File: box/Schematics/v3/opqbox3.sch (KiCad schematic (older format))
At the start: 2 parts, among them J1 Conn_01x02_Male, J2 Conn_01x02_Male

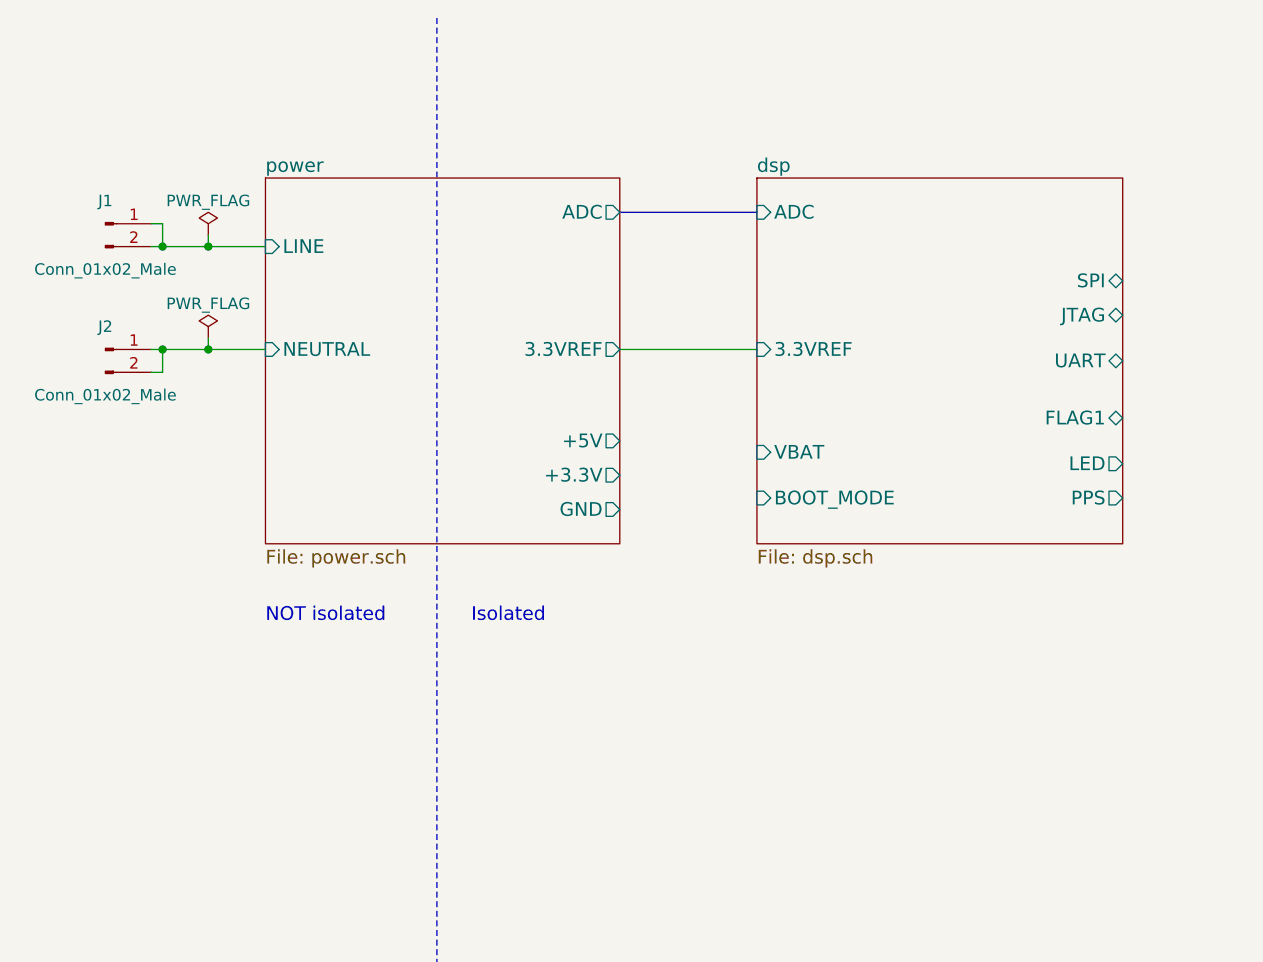
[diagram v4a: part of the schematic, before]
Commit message: create connectors sheet
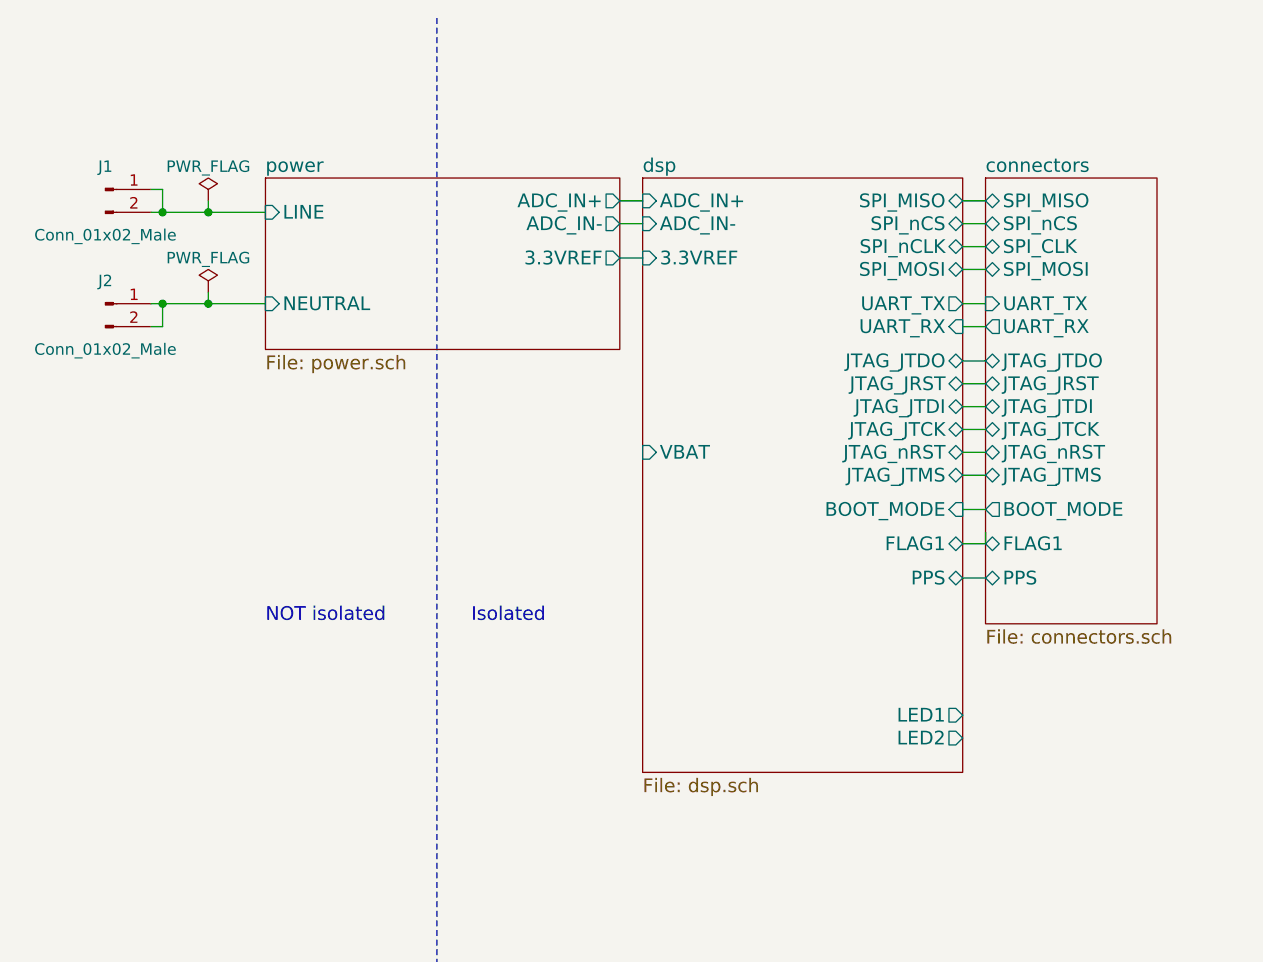
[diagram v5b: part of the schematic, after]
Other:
- moved on the sheet: J1, J2
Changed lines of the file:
@@
 LIBS:power
 LIBS:conn
-LIBS:contrib
-LIBS:stm32
 LIBS:opqbox3-cache
 EELAYER 25 0
@@
 $Descr A4 11693 8268
 encoding utf-8
-Sheet 1 3
+Sheet 1 4
 Title ""
 Date ""
@@
 $EndDescr
 $Sheet
-S 2150 1200 1550 1600
+S 2150 1200 1550 750
 U 5A829EE9
 F0 "power" 60
 F1 "power.sch" 60
-F2 "LINE" I L 2150 1500 60
-F3 "NEUTRAL" I L 2150 1950 60
-F4 "+3.3V" O R 3700 2500 60
-F5 "+5V" O R 3700 2350 60
-F6 "GND" O R 3700 2650 60
-F7 "3.3VREF" O R 3700 1950 60
-F8 "ADC" O R 3700 1350 60
+F2 "LINE" I L 2150 1350 60
+F3 "NEUTRAL" I L 2150 1750 60
+F4 "3.3VREF" O R 3700 1550 60
+F5 "ADC_IN-" O R 3700 1400 60
+F6 "ADC_IN+" O R 3700 1300 60
 $EndSheet
-Wire Notes Line
-	2900 500  2900 7750
 $Comp
 L Conn_01x02_Male J1
 U 1 1 5A82EE79
-P 1450 1400
-F 0 "J1" H 1450 1500 50  0000 C CNN
-F 1 "Conn_01x02_Male" H 1450 1200 50  0000 C CNN
-F 2 "" H 1450 1400 50  0001 C CNN
-F 3 "" H 1450 1400 50  0001 C CNN
-	1    1450 1400
+P 1450 1250
+F 0 "J1" H 1450 1350 50  0000 C CNN
+F 1 "Conn_01x02_Male" H 1450 1050 50  0000 C CNN
+F 2 "" H 1450 1250 50  0001 C CNN
+F 3 "" H 1450 1250 50  0001 C CNN
+	1    1450 1250
 	1    0    0    -1
 $EndComp
@@
 L Conn_01x02_Male J2
 U 1 1 5A82EEC2
-P 1450 1950
-F 0 "J2" H 1450 2050 50  0000 C CNN
-F 1 "Conn_01x02_Male" H 1450 1750 50  0000 C CNN
-F 2 "" H 1450 1950 50  0001 C CNN
-F 3 "" H 1450 1950 50  0001 C CNN
-	1    1450 1950
+P 1450 1750
+F 0 "J2" H 1450 1850 50  0000 C CNN
+F 1 "Conn_01x02_Male" H 1450 1550 50  0000 C CNN
+F 2 "" H 1450 1750 50  0001 C CNN
+F 3 "" H 1450 1750 50  0001 C CNN
+	1    1450 1750
 	1    0    0    -1
 $EndComp
-Wire Wire Line
-	1650 1400 1700 1400
-Wire Wire Line
-	1700 1400 1700 1500
-Wire Wire Line
-	1650 1500 2150 1500
-Connection ~ 1700 1500
-Wire Wire Line
-	1650 2050 1700 2050
-Wire Wire Line
-	1700 2050 1700 1950
-Wire Wire Line
-	1650 1950 2150 1950
-Connection ~ 1700 1950
 $Comp
 L PWR_FLAG #FLG01
 U 1 1 5A82F319
-P 1900 1450
-F 0 "#FLG01" H 1900 1525 50  0001 C CNN
-F 1 "PWR_FLAG" H 1900 1600 50  0000 C CNN
-F 2 "" H 1900 1450 50  0001 C CNN
-F 3 "" H 1900 1450 50  0001 C CNN
-	1    1900 1450
+P 1900 1300
+F 0 "#FLG01" H 1900 1375 50  0001 C CNN
+F 1 "PWR_FLAG" H 1900 1450 50  0000 C CNN
+F 2 "" H 1900 1300 50  0001 C CNN
+F 3 "" H 1900 1300 50  0001 C CNN
+	1    1900 1300
 	1    0    0    -1
 $EndComp
@@
 L PWR_FLAG #FLG02
 U 1 1 5A82F35B
-P 1900 1900
-F 0 "#FLG02" H 1900 1975 50  0001 C CNN
-F 1 "PWR_FLAG" H 1900 2050 50  0000 C CNN
-F 2 "" H 1900 1900 50  0001 C CNN
-F 3 "" H 1900 1900 50  0001 C CNN
-	1    1900 1900
+P 1900 1700
+F 0 "#FLG02" H 1900 1775 50  0001 C CNN
+F 1 "PWR_FLAG" H 1900 1850 50  0000 C CNN
+F 2 "" H 1900 1700 50  0001 C CNN
+F 3 "" H 1900 1700 50  0001 C CNN
+	1    1900 1700
 	1    0    0    -1
 $EndComp
-Wire Wire Line
-	1900 1900 1900 1950
-Connection ~ 1900 1950
-Wire Wire Line
-	1900 1450 1900 1500
-Connection ~ 1900 1500
 Text Notes 3050 3150 0    60   ~ 0
 Isolated
 Text Notes 2150 3150 0    60   ~ 0
 NOT isolated
+Wire Notes Line
+	2900 500  2900 7750
+Wire Wire Line
+	1650 1250 1700 1250
+Wire Wire Line
+	1700 1250 1700 1350
+Wire Wire Line
+	1650 1350 2150 1350
+Connection ~ 1700 1350
+Wire Wire Line
+	1650 1850 1700 1850
+Wire Wire Line
+	1700 1850 1700 1750
+Wire Wire Line
+	1650 1750 2150 1750
+Connection ~ 1700 1750
+Wire Wire Line
+	1900 1700 1900 1750
+Connection ~ 1900 1750
+Wire Wire Line
+	1900 1300 1900 1350
+Connection ~ 1900 1350
 $Sheet
-S 4300 1200 1600 1600
+S 5300 1200 750  1950
+U 5A8506F3
+F0 "connectors" 60
+F1 "connectors.sch" 60
+F2 "SPI_MISO" B L 5300 1300 60
+F3 "SPI_MOSI" B L 5300 1600 60
+F4 "SPI_nCS" B L 5300 1400 60
+F5 "SPI_CLK" B L 5300 1500 60
+F6 "JTAG_nRST" B L 5300 2400 60
+F7 "BOOT_MODE" O L 5300 2650 60
+F8 "UART_RX" O L 5300 1850 60
+F9 "UART_TX" I L 5300 1750 60
+F10 "FLAG1" B L 5300 2800 60
+F11 "JTAG_JRST" B L 5300 2100 60
+F12 "JTAG_JTCK" B L 5300 2300 60
+F13 "JTAG_JTDI" B L 5300 2200 60
+F14 "JTAG_JTDO" B L 5300 2000 60
+F15 "JTAG_JTMS" B L 5300 2500 60
+F16 "PPS" B L 5300 2950 60
+$EndSheet
+Wire Wire Line
+	5300 2750 5300 2800
+Wire Wire Line
+	5300 2800 5200 2800
+Wire Wire Line
+	5200 2650 5300 2650
+Wire Wire Line
+	5200 2500 5300 2500
+Wire Wire Line
+	5200 2400 5300 2400
+Wire Wire Line
+	5200 2300 5300 2300
+Wire Wire Line
+	5200 2200 5300 2200
+Wire Wire Line
+	5200 2100 5300 2100
+Wire Wire Line
+	5200 2000 5300 2000
+Wire Wire Line
+	5200 1850 5300 1850
+Wire Wire Line
+	5300 1750 5200 1750
+Wire Wire Line
+	5200 1600 5300 1600
+Wire Wire Line
+	5200 1500 5300 1500
+Wire Wire Line
+	5200 1400 5300 1400
+Wire Wire Line
+	5200 1300 5300 1300
+$Sheet
+S 3800 1200 1400 2600
 U 5A835DDE
 F0 "dsp" 60
 F1 "dsp.sch" 60
-F2 "3.3VREF" I L 4300 1950 60
-F3 "SPI" B R 5900 1650 60
-F4 "JTAG" B R 5900 1800 60
-F5 "UART" B R 5900 2000 60
-F6 "PPS" O R 5900 2600 60
-F7 "LED" O R 5900 2450 60
-F8 "BOOT_MODE" I L 4300 2600 60
-F9 "VBAT" I L 4300 2400 60
-F10 "FLAG1" B R 5900 2250 60
-F11 "ADC" I L 4300 1350 60
+F2 "BOOT_MODE" I R 5200 2650 60
+F3 "VBAT" I L 3800 2400 60
+F4 "SPI_MISO" B R 5200 1300 60
+F5 "LED1" O R 5200 3550 60
+F6 "FLAG1" B R 5200 2800 60
+F7 "ADC_IN+" I L 3800 1300 60
+F8 "SPI_nCS" B R 5200 1400 60
+F9 "SPI_nCLK" B R 5200 1500 60
+F10 "SPI_MOSI" B R 5200 1600 60
+F11 "ADC_IN-" I L 3800 1400 60
+F12 "LED2" O R 5200 3650 60
+F13 "JTAG_JTDO" B R 5200 2000 60
+F14 "JTAG_JRST" B R 5200 2100 60
+F15 "JTAG_JTDI" B R 5200 2200 60
+F16 "JTAG_JTCK" B R 5200 2300 60
+F17 "JTAG_nRST" B R 5200 2400 60
+F18 "JTAG_JTMS" B R 5200 2500 60
+F19 "3.3VREF" I L 3800 1550 60
+F20 "UART_RX" I R 5200 1850 60
+F21 "UART_TX" O R 5200 1750 60
+F22 "PPS" B R 5200 2950 60
 $EndSheet
 Wire Wire Line
-	3700 1950 4300 1950
-Wire Bus Line
-	3700 1350 4300 1350
+	5200 2950 5300 2950
+Wire Wire Line
+	3700 1300 3800 1300
+Wire Wire Line
+	3700 1400 3800 1400
+Wire Wire Line
+	3700 1550 3800 1550
 $EndSCHEMATC

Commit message: create io schematics
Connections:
- no-connect marks 0 -> 1
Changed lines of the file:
@@
 $EndDescr
 $Sheet
-S 2150 1200 1550 750
+S 2150 1200 1050 750
 U 5A829EE9
 F0 "power" 60
@@
 F2 "LINE" I L 2150 1350 60
 F3 "NEUTRAL" I L 2150 1750 60
-F4 "3.3VREF" O R 3700 1550 60
-F5 "ADC_IN-" O R 3700 1400 60
-F6 "ADC_IN+" O R 3700 1300 60
+F4 "3.3VREF" O R 3200 1550 60
+F5 "ADC_IN-" O R 3200 1400 60
+F6 "ADC_IN+" O R 3200 1300 60
 $EndSheet
 $Comp
@@
 	1    0    0    -1
 $EndComp
-Text Notes 3050 3150 0    60   ~ 0
+Text Notes 2800 800  0    60   ~ 0
 Isolated
-Text Notes 2150 3150 0    60   ~ 0
+Text Notes 2050 800  0    60   ~ 0
 NOT isolated
+$Sheet
+S 4800 1200 750  2300
+U 5A8506F3
+F0 "io" 60
+F1 "io.sch" 60
+F2 "SPI_MISO" B L 4800 1300 60
+F3 "SPI_MOSI" B L 4800 1600 60
+F4 "SPI_nCS" B L 4800 1400 60
+F5 "SPI_CLK" B L 4800 1500 60
+F6 "JTAG_nRST" B L 4800 2400 60
+F7 "BOOT_MODE" O L 4800 2650 60
+F8 "UART_RX" O L 4800 1850 60
+F9 "UART_TX" I L 4800 1750 60
+F10 "FLAG1" B L 4800 2800 60
+F11 "JTAG_JRST" B L 4800 2100 60
+F12 "JTAG_JTCK" B L 4800 2300 60
+F13 "JTAG_JTDI" B L 4800 2200 60
+F14 "JTAG_JTDO" B L 4800 2000 60
+F15 "JTAG_JTMS" B L 4800 2500 60
+F16 "PPS" B L 4800 2950 60
+F17 "LED1" I L 4800 3300 60
+F18 "LED2" I L 4800 3400 60
+$EndSheet
+$Sheet
+S 3300 1200 1400 2600
+U 5A835DDE
+F0 "dsp" 60
+F1 "dsp.sch" 60
+F2 "BOOT_MODE" I R 4700 2650 60
+F3 "VBAT" I L 3300 1850 60
+F4 "SPI_MISO" B R 4700 1300 60
+F5 "LED1" O R 4700 3300 60
+F6 "FLAG1" B R 4700 2800 60
+F7 "ADC_IN+" I L 3300 1300 60
+F8 "SPI_nCS" B R 4700 1400 60
+F9 "SPI_nCLK" B R 4700 1500 60
+F10 "SPI_MOSI" B R 4700 1600 60
+F11 "ADC_IN-" I L 3300 1400 60
+F12 "LED2" O R 4700 3400 60
+F13 "JTAG_JTDO" B R 4700 2000 60
+F14 "JTAG_JRST" B R 4700 2100 60
+F15 "JTAG_JTDI" B R 4700 2200 60
+F16 "JTAG_JTCK" B R 4700 2300 60
+F17 "JTAG_nRST" B R 4700 2400 60
+F18 "JTAG_JTMS" B R 4700 2500 60
+F19 "3.3VREF" I L 3300 1550 60
+F20 "UART_RX" I R 4700 1850 60
+F21 "UART_TX" O R 4700 1750 60
+F22 "PPS" B R 4700 2950 60
+$EndSheet
 Wire Notes Line
-	2900 500  2900 7750
+	2700 500  2700 7750
 Wire Wire Line
 	1650 1250 1700 1250
@@
 	1900 1300 1900 1350
 Connection ~ 1900 1350
-$Sheet
-S 5300 1200 750  1950
-U 5A8506F3
-F0 "connectors" 60
-F1 "connectors.sch" 60
-F2 "SPI_MISO" B L 5300 1300 60
-F3 "SPI_MOSI" B L 5300 1600 60
-F4 "SPI_nCS" B L 5300 1400 60
-F5 "SPI_CLK" B L 5300 1500 60
-F6 "JTAG_nRST" B L 5300 2400 60
-F7 "BOOT_MODE" O L 5300 2650 60
-F8 "UART_RX" O L 5300 1850 60
-F9 "UART_TX" I L 5300 1750 60
-F10 "FLAG1" B L 5300 2800 60
-F11 "JTAG_JRST" B L 5300 2100 60
-F12 "JTAG_JTCK" B L 5300 2300 60
-F13 "JTAG_JTDI" B L 5300 2200 60
-F14 "JTAG_JTDO" B L 5300 2000 60
-F15 "JTAG_JTMS" B L 5300 2500 60
-F16 "PPS" B L 5300 2950 60
-$EndSheet
 Wire Wire Line
-	5300 2750 5300 2800
+	4800 2750 4800 2800
 Wire Wire Line
-	5300 2800 5200 2800
+	4800 2800 4700 2800
 Wire Wire Line
-	5200 2650 5300 2650
+	4700 2650 4800 2650
 Wire Wire Line
-	5200 2500 5300 2500
+	4700 2500 4800 2500
 Wire Wire Line
-	5200 2400 5300 2400
+	4700 2400 4800 2400
 Wire Wire Line
-	5200 2300 5300 2300
+	4700 2300 4800 2300
 Wire Wire Line
-	5200 2200 5300 2200
+	4700 2200 4800 2200
 Wire Wire Line
-	5200 2100 5300 2100
+	4700 2100 4800 2100
 Wire Wire Line
-	5200 2000 5300 2000
+	4700 2000 4800 2000
 Wire Wire Line
-	5200 1850 5300 1850
+	4700 1850 4800 1850
 Wire Wire Line
-	5300 1750 5200 1750
+	4800 1750 4700 1750
 Wire Wire Line
-	5200 1600 5300 1600
+	4700 1600 4800 1600
 Wire Wire Line
-	5200 1500 5300 1500
+	4700 1500 4800 1500
 Wire Wire Line
-	5200 1400 5300 1400
+	4700 1400 4800 1400
 Wire Wire Line
-	5200 1300 5300 1300
-$Sheet
-S 3800 1200 1400 2600
-U 5A835DDE
-F0 "dsp" 60
-F1 "dsp.sch" 60
-F2 "BOOT_MODE" I R 5200 2650 60
-F3 "VBAT" I L 3800 2400 60
-F4 "SPI_MISO" B R 5200 1300 60
-F5 "LED1" O R 5200 3550 60
-F6 "FLAG1" B R 5200 2800 60
-F7 "ADC_IN+" I L 3800 1300 60
-F8 "SPI_nCS" B R 5200 1400 60
-F9 "SPI_nCLK" B R 5200 1500 60
-F10 "SPI_MOSI" B R 5200 1600 60
-F11 "ADC_IN-" I L 3800 1400 60
-F12 "LED2" O R 5200 3650 60
-F13 "JTAG_JTDO" B R 5200 2000 60
-F14 "JTAG_JRST" B R 5200 2100 60
-F15 "JTAG_JTDI" B R 5200 2200 60
-F16 "JTAG_JTCK" B R 5200 2300 60
-F17 "JTAG_nRST" B R 5200 2400 60
-F18 "JTAG_JTMS" B R 5200 2500 60
-F19 "3.3VREF" I L 3800 1550 60
-F20 "UART_RX" I R 5200 1850 60
-F21 "UART_TX" O R 5200 1750 60
-F22 "PPS" B R 5200 2950 60
-$EndSheet
+	4700 1300 4800 1300
 Wire Wire Line
-	5200 2950 5300 2950
+	4700 2950 4800 2950
 Wire Wire Line
-	3700 1300 3800 1300
+	3200 1300 3300 1300
 Wire Wire Line
-	3700 1400 3800 1400
+	3200 1400 3300 1400
 Wire Wire Line
-	3700 1550 3800 1550
+	3200 1550 3300 1550
+Wire Wire Line
+	4700 3300 4800 3300
+Wire Wire Line
+	4700 3400 4800 3400
+NoConn ~ 3300 1850
 $EndSCHEMATC

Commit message: start layout
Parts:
- J1, J2: footprint (none) -> opqbox3:FastonTab
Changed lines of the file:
@@
 EESchema Schematic File Version 2
+LIBS:opqbox3-rescue
 LIBS:opqbox3
 LIBS:device
@@
 $EndDescr
 $Sheet
-S 2150 1200 1050 750
+S 2150 1200 1100 750
 U 5A829EE9
 F0 "power" 60
@@
 F2 "LINE" I L 2150 1350 60
 F3 "NEUTRAL" I L 2150 1750 60
-F4 "3.3VREF" O R 3200 1550 60
-F5 "ADC_IN-" O R 3200 1400 60
-F6 "ADC_IN+" O R 3200 1300 60
+F4 "3.3VREF" O R 3250 1550 60
+F5 "ADC_IN-" O R 3250 1400 60
+F6 "ADC_IN+" O R 3250 1300 60
 $EndSheet
-$Comp
-L Conn_01x02_Male J1
-U 1 1 5A82EE79
-P 1450 1250
-F 0 "J1" H 1450 1350 50  0000 C CNN
-F 1 "Conn_01x02_Male" H 1450 1050 50  0000 C CNN
-F 2 "" H 1450 1250 50  0001 C CNN
-F 3 "" H 1450 1250 50  0001 C CNN
-	1    1450 1250
-	1    0    0    -1
-$EndComp
-$Comp
-L Conn_01x02_Male J2
-U 1 1 5A82EEC2
-P 1450 1750
-F 0 "J2" H 1450 1850 50  0000 C CNN
-F 1 "Conn_01x02_Male" H 1450 1550 50  0000 C CNN
-F 2 "" H 1450 1750 50  0001 C CNN
-F 3 "" H 1450 1750 50  0001 C CNN
-	1    1450 1750
-	1    0    0    -1
-$EndComp
 $Comp
 L PWR_FLAG #FLG01
@@
 NOT isolated
 $Sheet
-S 4800 1200 750  2300
+S 4850 1200 750  2300
 U 5A8506F3
 F0 "io" 60
 F1 "io.sch" 60
-F2 "SPI_MISO" B L 4800 1300 60
-F3 "SPI_MOSI" B L 4800 1600 60
-F4 "SPI_nCS" B L 4800 1400 60
-F5 "SPI_CLK" B L 4800 1500 60
-F6 "JTAG_nRST" B L 4800 2400 60
-F7 "BOOT_MODE" O L 4800 2650 60
-F8 "UART_RX" O L 4800 1850 60
-F9 "UART_TX" I L 4800 1750 60
-F10 "FLAG1" B L 4800 2800 60
-F11 "JTAG_JRST" B L 4800 2100 60
-F12 "JTAG_JTCK" B L 4800 2300 60
-F13 "JTAG_JTDI" B L 4800 2200 60
-F14 "JTAG_JTDO" B L 4800 2000 60
-F15 "JTAG_JTMS" B L 4800 2500 60
-F16 "PPS" B L 4800 2950 60
-F17 "LED1" I L 4800 3300 60
-F18 "LED2" I L 4800 3400 60
+F2 "SPI_MISO" B L 4850 1300 60
+F3 "SPI_MOSI" B L 4850 1600 60
+F4 "SPI_nCS" B L 4850 1400 60
+F5 "SPI_CLK" B L 4850 1500 60
+F6 "JTAG_nRST" B L 4850 2400 60
+F7 "BOOT_MODE" O L 4850 2650 60
+F8 "UART_RX" O L 4850 1850 60
+F9 "UART_TX" I L 4850 1750 60
+F10 "FLAG1" B L 4850 2800 60
+F11 "JTAG_JRST" B L 4850 2100 60
+F12 "JTAG_JTCK" B L 4850 2300 60
+F13 "JTAG_JTDI" B L 4850 2200 60
+F14 "JTAG_JTDO" B L 4850 2000 60
+F15 "JTAG_JTMS" B L 4850 2500 60
+F16 "PPS" B L 4850 2950 60
+F17 "LED1" I L 4850 3300 60
+F18 "LED2" I L 4850 3400 60
 $EndSheet
 $Sheet
-S 3300 1200 1400 2600
+S 3350 1200 1400 2600
 U 5A835DDE
 F0 "dsp" 60
 F1 "dsp.sch" 60
-F2 "BOOT_MODE" I R 4700 2650 60
-F3 "VBAT" I L 3300 1850 60
-F4 "SPI_MISO" B R 4700 1300 60
-F5 "LED1" O R 4700 3300 60
-F6 "FLAG1" B R 4700 2800 60
-F7 "ADC_IN+" I L 3300 1300 60
-F8 "SPI_nCS" B R 4700 1400 60
-F9 "SPI_nCLK" B R 4700 1500 60
-F10 "SPI_MOSI" B R 4700 1600 60
-F11 "ADC_IN-" I L 3300 1400 60
-F12 "LED2" O R 4700 3400 60
-F13 "JTAG_JTDO" B R 4700 2000 60
-F14 "JTAG_JRST" B R 4700 2100 60
-F15 "JTAG_JTDI" B R 4700 2200 60
-F16 "JTAG_JTCK" B R 4700 2300 60
-F17 "JTAG_nRST" B R 4700 2400 60
-F18 "JTAG_JTMS" B R 4700 2500 60
-F19 "3.3VREF" I L 3300 1550 60
-F20 "UART_RX" I R 4700 1850 60
-F21 "UART_TX" O R 4700 1750 60
-F22 "PPS" B R 4700 2950 60
+F2 "BOOT_MODE" I R 4750 2650 60
+F3 "VBAT" I L 3350 1850 60
+F4 "SPI_MISO" B R 4750 1300 60
+F5 "LED1" O R 4750 3300 60
+F6 "FLAG1" B R 4750 2800 60
+F7 "ADC_IN+" I L 3350 1300 60
+F8 "SPI_nCS" B R 4750 1400 60
+F9 "SPI_nCLK" B R 4750 1500 60
+F10 "SPI_MOSI" B R 4750 1600 60
+F11 "ADC_IN-" I L 3350 1400 60
+F12 "LED2" O R 4750 3400 60
+F13 "JTAG_JTDO" B R 4750 2000 60
+F14 "JTAG_JRST" B R 4750 2100 60
+F15 "JTAG_JTDI" B R 4750 2200 60
+F16 "JTAG_JTCK" B R 4750 2300 60
+F17 "JTAG_nRST" B R 4750 2400 60
+F18 "JTAG_JTMS" B R 4750 2500 60
+F19 "3.3VREF" I L 3350 1550 60
+F20 "UART_RX" I R 4750 1850 60
+F21 "UART_TX" O R 4750 1750 60
+F22 "PPS" B R 4750 2950 60
 $EndSheet
 Wire Notes Line
 	2700 500  2700 7750
 Wire Wire Line
-	1650 1250 1700 1250
-Wire Wire Line
-	1700 1250 1700 1350
-Wire Wire Line
 	1650 1350 2150 1350
-Connection ~ 1700 1350
-Wire Wire Line
-	1650 1850 1700 1850
-Wire Wire Line
-	1700 1850 1700 1750
 Wire Wire Line
 	1650 1750 2150 1750
-Connection ~ 1700 1750
 Wire Wire Line
 	1900 1700 1900 1750
@@
 Connection ~ 1900 1350
 Wire Wire Line
-	4800 2750 4800 2800
+	4850 2750 4850 2800
 Wire Wire Line
-	4800 2800 4700 2800
+	4850 2800 4750 2800
 Wire Wire Line
-	4700 2650 4800 2650
+	4750 2650 4850 2650
 Wire Wire Line
-	4700 2500 4800 2500
+	4750 2500 4850 2500
 Wire Wire Line
-	4700 2400 4800 2400
+	4750 2400 4850 2400
 Wire Wire Line
-	4700 2300 4800 2300
+	4750 2300 4850 2300
 Wire Wire Line
-	4700 2200 4800 2200
+	4750 2200 4850 2200
 Wire Wire Line
-	4700 2100 4800 2100
+	4750 2100 4850 2100
 Wire Wire Line
-	4700 2000 4800 2000
+	4750 2000 4850 2000
 Wire Wire Line
-	4700 1850 4800 1850
+	4750 1850 4850 1850
 Wire Wire Line
-	4800 1750 4700 1750
+	4850 1750 4750 1750
 Wire Wire Line
-	4700 1600 4800 1600
+	4750 1600 4850 1600
 Wire Wire Line
-	4700 1500 4800 1500
+	4750 1500 4850 1500
 Wire Wire Line
-	4700 1400 4800 1400
+	4750 1400 4850 1400
 Wire Wire Line
-	4700 1300 4800 1300
+	4750 1300 4850 1300
 Wire Wire Line
-	4700 2950 4800 2950
+	4750 2950 4850 2950
 Wire Wire Line
-	3200 1300 3300 1300
+	3250 1300 3350 1300
 Wire Wire Line
-	3200 1400 3300 1400
+	3250 1400 3350 1400
 Wire Wire Line
-	3200 1550 3300 1550
+	3250 1550 3350 1550
 Wire Wire Line
-	4700 3300 4800 3300
+	4750 3300 4850 3300
 Wire Wire Line
-	4700 3400 4800 3400
-NoConn ~ 3300 1850
+	4750 3400 4850 3400
+NoConn ~ 3350 1850
+$Comp
+L Conn_01x02_Male J1
+U 1 1 5A83BEC0
+P 1450 1250
+F 0 "J1" H 1450 1350 50  0000 C CNN
+F 1 "Conn_01x02_Male" H 1450 1050 50  0000 C CNN
+F 2 "opqbox3:FastonTab" H 1450 1250 50  0001 C CNN
+F 3 "" H 1450 1250 50  0001 C CNN
+	1    1450 1250
+	1    0    0    -1
+$EndComp
+$Comp
+L Conn_01x02_Male J2
+U 1 1 5A83C177
+P 1450 1650
+F 0 "J2" H 1450 1750 50  0000 C CNN
+F 1 "Conn_01x02_Male" H 1450 1450 50  0000 C CNN
+F 2 "opqbox3:FastonTab" H 1450 1650 50  0001 C CNN
+F 3 "" H 1450 1650 50  0001 C CNN
+	1    1450 1650
+	1    0    0    -1
+$EndComp
+Wire Wire Line
+	1650 1250 1700 1250
+Wire Wire Line
+	1700 1250 1700 1350
+Connection ~ 1700 1350
+Wire Wire Line
+	1650 1650 1700 1650
+Wire Wire Line
+	1700 1650 1700 1750
+Connection ~ 1700 1750
 $EndSCHEMATC
